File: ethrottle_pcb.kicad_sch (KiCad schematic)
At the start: 49 parts

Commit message: update connections
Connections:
- net +12V: now also J?.1
- net Brake: now also J?.4; no longer J?.2
- net GND: now also J?.2; no longer J?.1
- net Output: now also J?.5; no longer J?.4
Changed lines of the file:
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@@
     (effects (font (size 1.27 1.27)) (justify left bottom))
   )
-  (global_label "Throttle" (shape input) (at 31.75 132.08 180) (fields_autoplaced)
+  (global_label "Throttle" (shape input) (at 31.75 134.62 180) (fields_autoplaced)
     (effects (font (size 1.27 1.27)) (justify right))
-    (property "Intersheet References" "${INTERSHEET_REFS}" (id 0) (at 22.0798 132.1594 0)
+    (property "Intersheet References" "${INTERSHEET_REFS}" (id 0) (at 22.0798 134.6994 0)
       (effects (font (size 1.27 1.27)) (justify right) hide)
     )
@@
     )
   )
-  (global_label "Output" (shape input) (at 31.75 137.16 180) (fields_autoplaced)
+  (global_label "Output" (shape input) (at 31.75 139.7 180) (fields_autoplaced)
     (effects (font (size 1.27 1.27)) (justify right))
-    (property "Intersheet References" "${INTERSHEET_REFS}" (id 0) (at 23.1079 137.0806 0)
+    (property "Intersheet References" "${INTERSHEET_REFS}" (id 0) (at 23.1079 139.6206 0)
       (effects (font (size 1.27 1.27)) (justify right) hide)
     )
@@
     )
   )
-  (global_label "Brake" (shape input) (at 31.75 134.62 180) (fields_autoplaced)
+  (global_label "Brake" (shape input) (at 31.75 137.16 180) (fields_autoplaced)
     (effects (font (size 1.27 1.27)) (justify right))
-    (property "Intersheet References" "${INTERSHEET_REFS}" (id 0) (at 24.015 134.5406 0)
+    (property "Intersheet References" "${INTERSHEET_REFS}" (id 0) (at 24.015 137.0806 0)
       (effects (font (size 1.27 1.27)) (justify right) hide)
     )
@@
     (pin "2")
   )
+  (symbol (lib_id "power:+12V") (at 31.75 129.54 90) (unit 1)
+    (in_bom yes) (on_board yes)
+    (property "Reference" "#PWR?" (id 0) (at 35.56 129.54 0)
+      (effects (font (size 1.27 1.27)) hide)
+    )
+    (property "Value" "+12V" (id 1) (at 26.67 128.27 90))
+    (property "Footprint" "" (id 2) (at 31.75 129.54 0)
+      (effects (font (size 1.27 1.27)) hide)
+    )
+    (property "Datasheet" "" (id 3) (at 31.75 129.54 0)
+      (effects (font (size 1.27 1.27)) hide)
+    )
+    (pin "1")
+  )
   (symbol (lib_id "Device:R") (at 167.64 45.72 0) (unit 1)
     (in_bom yes) (on_board yes) (fields_autoplaced)
@@
     (pin "4")
   )
-  (symbol (lib_id "power:GND") (at 31.75 129.54 270) (unit 1)
-    (in_bom yes) (on_board yes)
-    (property "Reference" "#PWR?" (id 0) (at 25.4 129.54 0)
-      (effects (font (size 1.27 1.27)) hide)
-    )
-    (property "Value" "GND" (id 1) (at 25.4 128.27 90)
-      (effects (font (size 1.27 1.27)) (justify left))
-    )
-    (property "Footprint" "" (id 2) (at 31.75 129.54 0)
-      (effects (font (size 1.27 1.27)) hide)
-    )
-    (property "Datasheet" "" (id 3) (at 31.75 129.54 0)
+  (symbol (lib_id "power:GND") (at 31.75 132.08 270) (unit 1)
+    (in_bom yes) (on_board yes)
+    (property "Reference" "#PWR?" (id 0) (at 25.4 132.08 0)
+      (effects (font (size 1.27 1.27)) hide)
+    )
+    (property "Value" "GND" (id 1) (at 25.4 130.81 90)
+      (effects (font (size 1.27 1.27)) (justify left))
+    )
+    (property "Footprint" "" (id 2) (at 31.75 132.08 0)
+      (effects (font (size 1.27 1.27)) hide)
+    )
+    (property "Datasheet" "" (id 3) (at 31.75 132.08 0)
       (effects (font (size 1.27 1.27)) hide)
     )
@@
       (reference "#PWR?") (unit 1) (value "GND") (footprint "")
     )
+    (path "/af4fe4c5-3121-44b8-959e-e5c992990974"
+      (reference "#PWR?") (unit 1) (value "+12V") (footprint "")
+    )
     (path "/c3affea8-6cb9-4035-a7f6-fd73cd47eeb6"

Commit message: update footprints
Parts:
- C?: footprint (none) -> Capacitor_SMD:C_0805_2012Metric
- R? (x22): footprint (none) -> Resistor_SMD:R_01005_0402Metric

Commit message: add footprints
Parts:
- C?: footprint (none) -> Capacitor_SMD:C_0805_2012Metric
- D? (x5): footprint (none) -> APGF0606SYKCGK-TT-C2:APGF0606SYKCGKTTC2
- U? (x8): footprint (none) -> LM324N_NOPB:DIP825W47P254L1917H533Q14
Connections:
- net GND: no longer J?.2

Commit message: layout in progress
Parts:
- D1, D11, D2, D3, D4: renamed from D?; footprint APGF0606SYKCGK-TT-C2:APGF0606SYKCGKTTC2 -> LED_SMD:LED_0402_1005Metric
- D10, D5, D6, D8, D9: renamed from D?; value 1N5401 -> CGRM4007-G; footprint Diode_THT:D_DO-201AD_P15.24mm_Horizontal -> Diode_SMD:D_SOD-123
- U2, U3: renamed from U?; footprint LM324N_NOPB:DIP825W47P254L1917H533Q14 -> LM324PWR:LM324PWR
- U2, U3: renamed from U?; footprint (none) -> LM324PWR:LM324PWR
- gave numbers to parts that had none: 29
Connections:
- net +5V is gone; now on net +12V: R16.1
- net Brake: no longer J1.3, R3.2, U2.12 (+), U2.3 (+)
- net GND: now also J1.2
- new net Throttle: J1.3, R3.2, U2.12 (+), U2.3 (+)

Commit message: update format
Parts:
- D7: value 1N5401 -> CGRM4007-G; footprint Diode_THT:D_DO-201AD_P15.24mm_Horizontal -> Diode_SMD:D_SOD-123
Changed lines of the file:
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@@
       (effects (font (size 1.27 1.27)) (justify left))
     )
-    (property "Value" "1N5401" (id 1) (at 158.75 43.18 0)
-      (effects (font (size 1.27 1.27)) (justify left))
-    )
-    (property "Footprint" "Diode_THT:D_DO-201AD_P15.24mm_Horizontal" (id 2) (at 156.845 46.99 0)
-      (effects (font (size 1.27 1.27)) hide)
-    )
-    (property "Datasheet" "http://www.vishay.com/docs/88516/1n5400.pdf" (id 3) (at 161.29 46.99 0)
+    (property "Value" "CGRM4007-G" (id 1) (at 158.75 43.18 0)
+      (effects (font (size 1.27 1.27)) (justify left))
+    )
+    (property "Footprint" "Diode_SMD:D_SOD-123" (id 2) (at 156.845 46.99 0)
+      (effects (font (size 1.27 1.27)) hide)
+    )
+    (property "Datasheet" "https://www.comchiptech.com/admin/files/product/CGRM4004-G%20Thru%20CGRM4007-G%20RevG.pdf" (id 3) (at 161.29 46.99 0)
       (effects (font (size 1.27 1.27)) hide)
     )
@@
     )
     (path "/735f6d1f-3aeb-4371-9f49-f96d24e8f53b"
-      (reference "D7") (unit 1) (value "1N5401") (footprint "Diode_THT:D_DO-201AD_P15.24mm_Horizontal")
+      (reference "D7") (unit 1) (value "CGRM4007-G") (footprint "Diode_SMD:D_SOD-123")
     )
     (path "/fb2cfbd8-3679-4e68-8a3a-75b3280455dc"

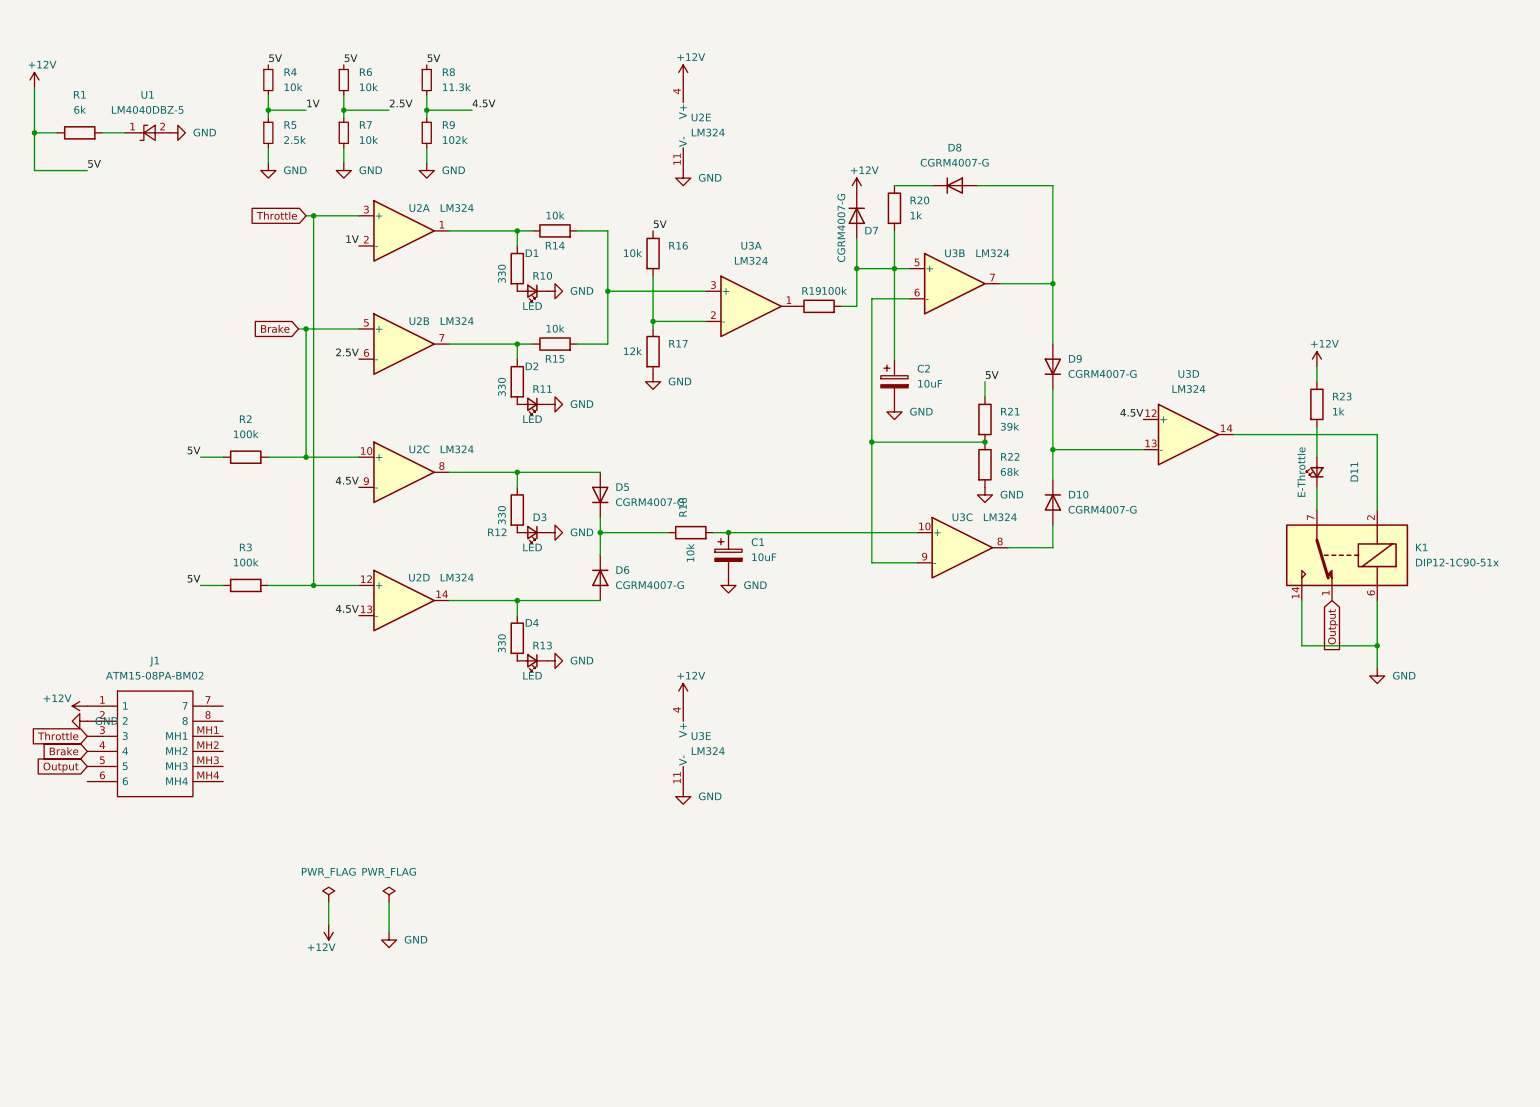
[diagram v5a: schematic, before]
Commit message: change labels
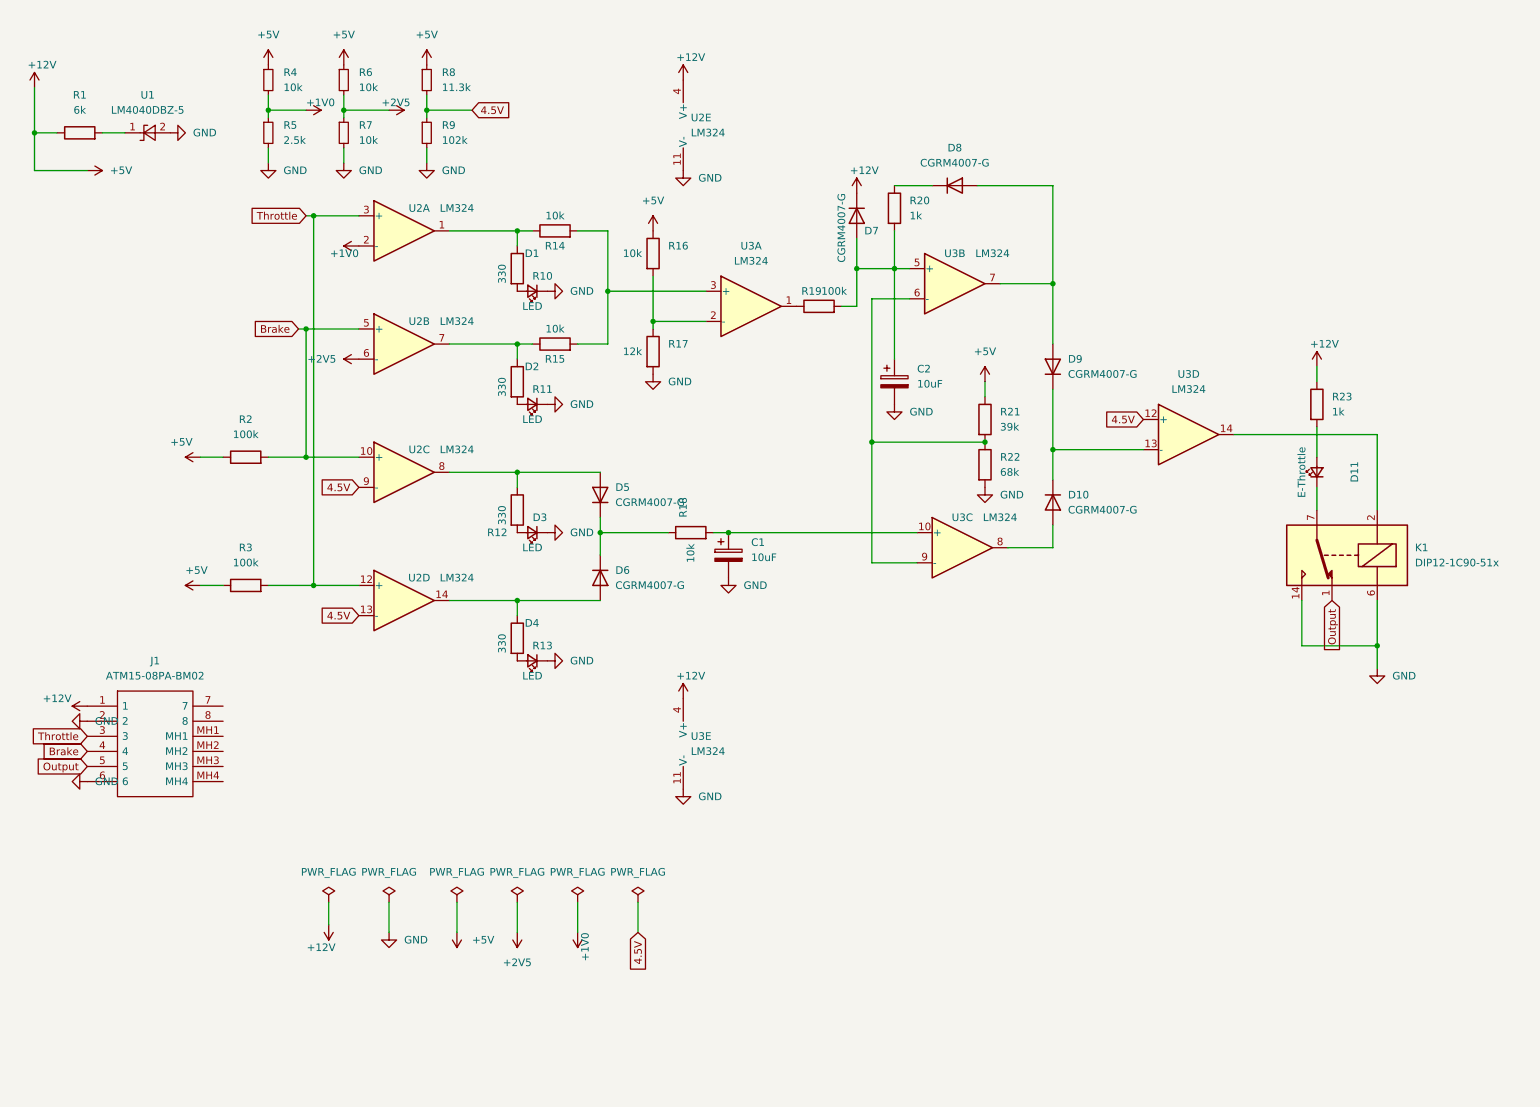
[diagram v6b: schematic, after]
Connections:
- net GND: now also J1.6
- net 1V renamed +1V0
- net 2.5V renamed +2V5

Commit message: update labels
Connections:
- net +12V: now also R1.2; no longer R1.1, R16.1, R2.1, R21.1, R3.1, R4.1, R6.1, R8.1
- net +5V: now reaches U1.1 (K)
- net +5V: now also R1.1, R16.1, R2.1, R21.1, R3.1, R4.1, R6.1, R8.1; no longer R1.2
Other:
- moved on the sheet: R1, U1

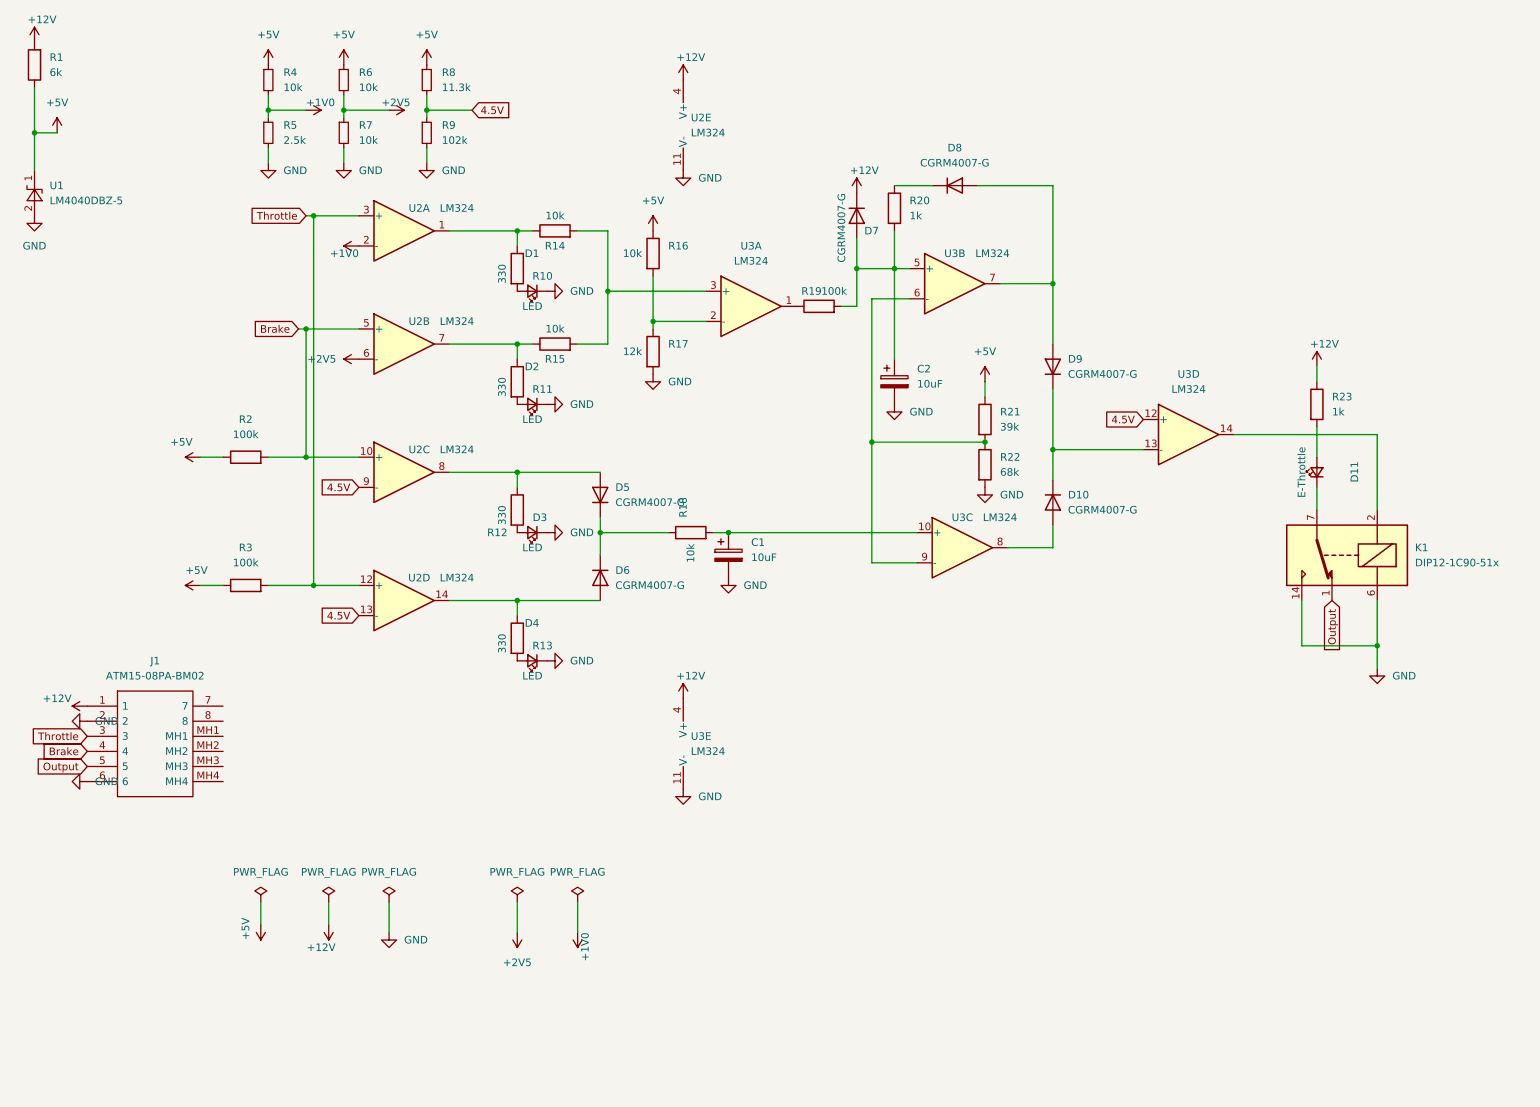
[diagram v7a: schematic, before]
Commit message: add lm358
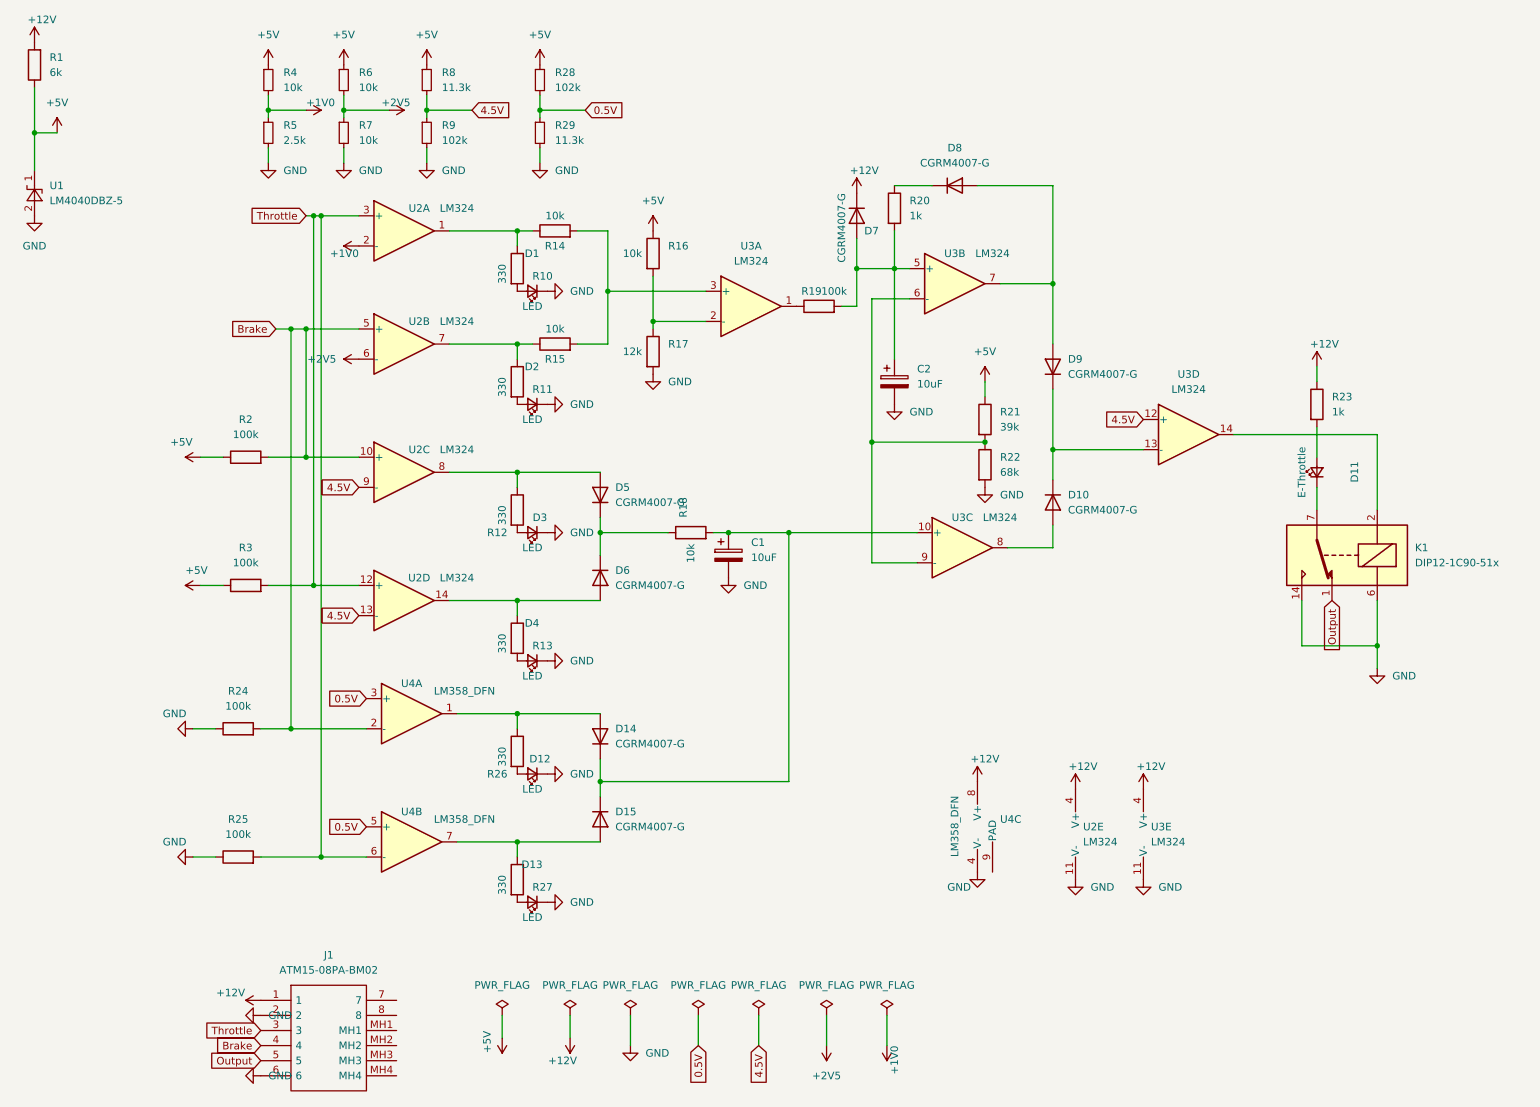
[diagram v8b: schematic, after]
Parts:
- added D12, D13: LED, LED_SMD:LED_0402_1005Metric, symbol Device:LED_Small
- added D14, D15: CGRM4007-G, Diode_SMD:D_SOD-123, symbol Diode:1N5401
- added R24, R25: 100k, Resistor_SMD:R_01005_0402Metric, symbol Device:R
- added R26, R27: 330, Resistor_SMD:R_01005_0402Metric, symbol Device:R
- added R28: 102k, Resistor_SMD:R_01005_0402Metric, symbol Device:R_Small
- added R29: 11.3k, Resistor_SMD:R_01005_0402Metric, symbol Device:R_Small
- added U4: LM358_DFN, Package_DFN_QFN:DFN-8-1EP_2x2mm_P0.5mm_EP1.05x1.75mm, symbol Amplifier_Operational:LM358_DFN
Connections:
- net +12V: now also U4.8 (V+)
- net +5V: now also R28.1
- net Brake: now also R24.2, U4.2 (-)
- net GND: now also D12.1 (K), D13.1 (K), R24.1, R25.1, R29.2, U4.4 (V-)
- net Throttle: now also R25.2, U4.6 (-)
- net at C1.1, R18.2, U3.10 (+): now also D14.1 (K), D15.1 (K)
- new net: D15.2 (A), R27.1, U4.7
- new net: D13.2 (A), R27.2
- new net: D14.2 (A), R26.1, U4.1
- new net: D12.2 (A), R26.2
- new net 0.5V: R28.2, R29.1, U4.3 (+), U4.5 (+)
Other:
- moved on the sheet: J1, U2E, U3E
